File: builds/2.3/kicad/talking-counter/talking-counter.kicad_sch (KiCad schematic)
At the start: 16 parts, among them IC1 TLV3501AIDR, J1 Conn_Coaxial

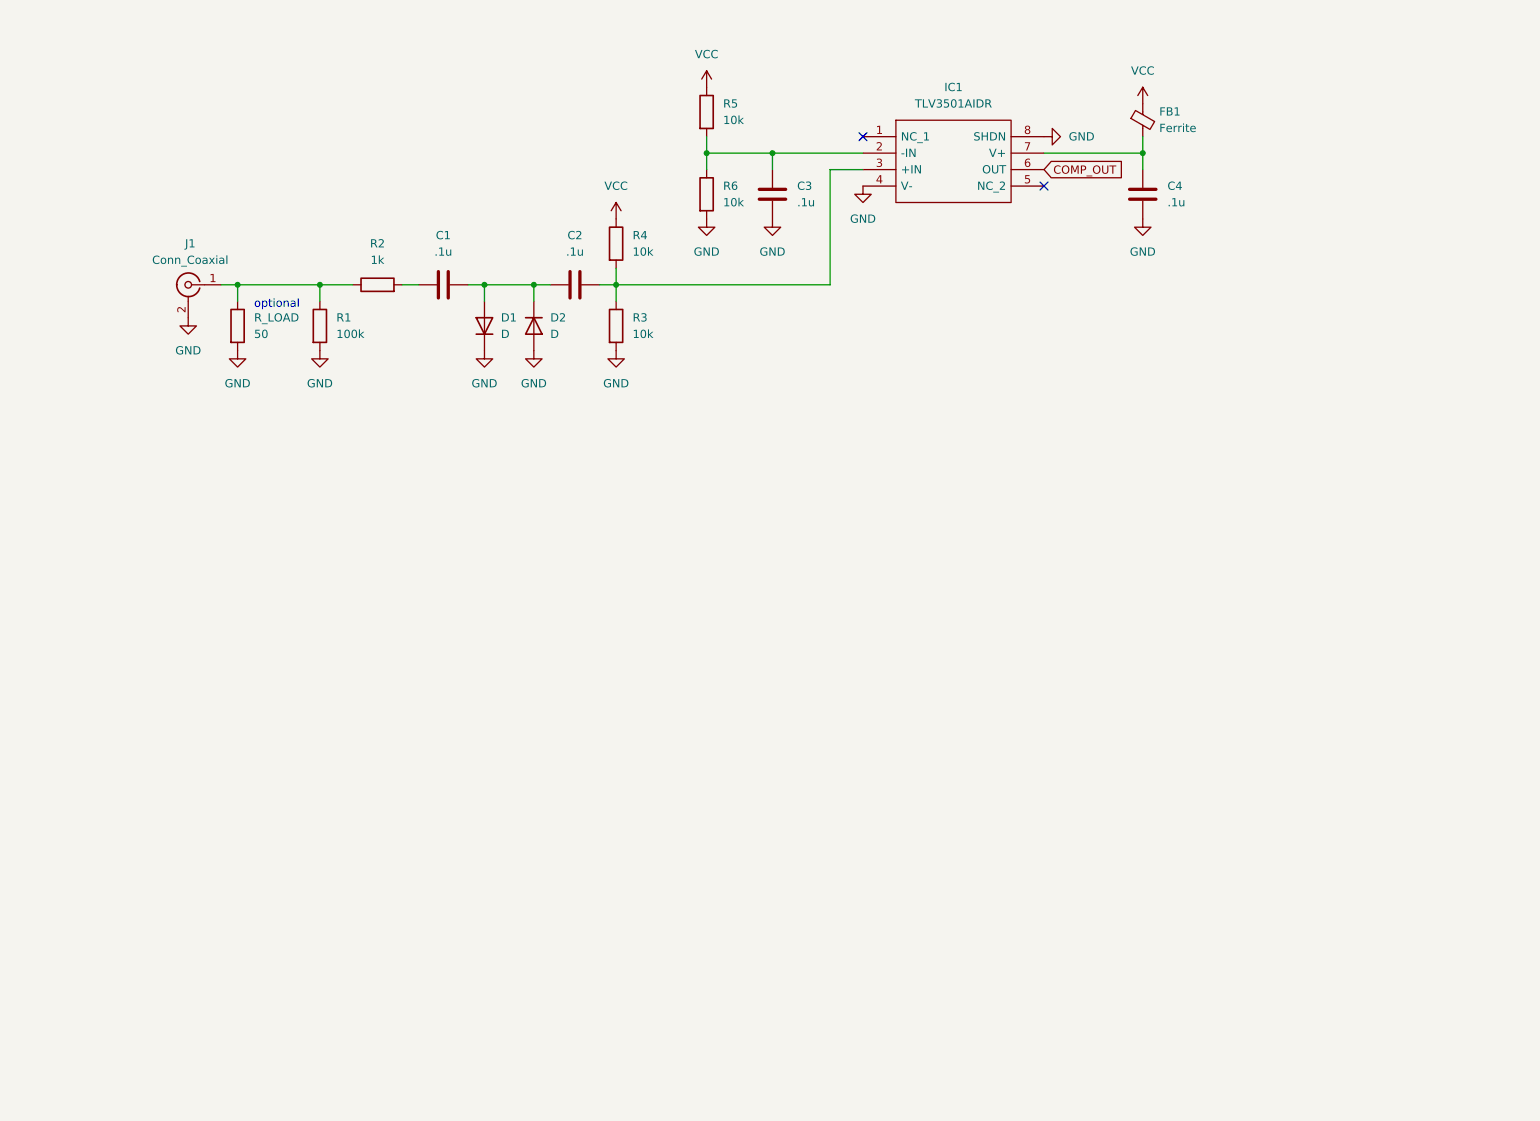
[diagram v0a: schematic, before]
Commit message: update schematic
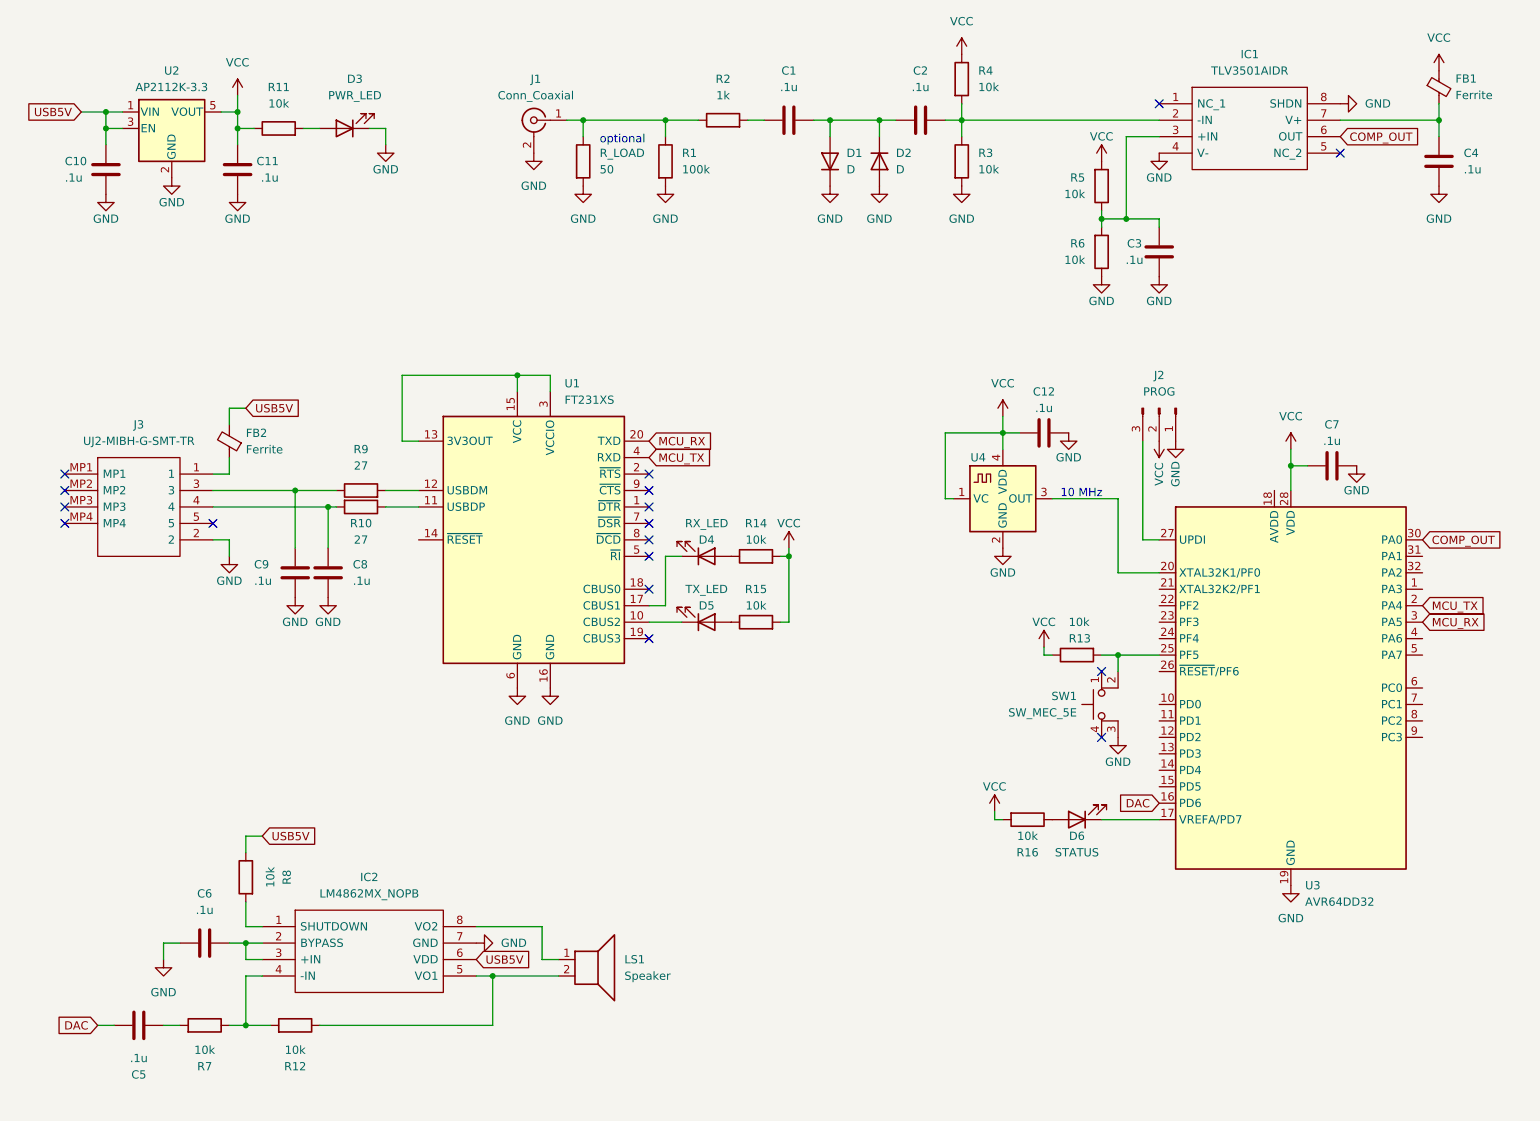
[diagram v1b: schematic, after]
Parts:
- added C10, C11, C12, C5, C6, C7, C8, C9: .1u, symbol Device:C
- added D3: PWR_LED, symbol Device:LED
- added D4: RX_LED, symbol Device:LED
- added D5: TX_LED, symbol Device:LED
- added D6: STATUS, symbol Device:LED
- added FB2: Ferrite, symbol Device:FerriteBead_Small
- added IC2: LM4862MX_NOPB, SOIC127P600X175-8N, symbol library loader:LM4862MX_NOPB
- added J2: PROG, symbol Connector:Conn_01x03_Pin
- added J3: UJ2-MIBH-G-SMT-TR, UJ2MIBHGSMTTR, symbol library loader:UJ2-MIBH-G-SMT-TR
- added LS1: Speaker, symbol Device:Speaker
- added R10, R9: 27, symbol Device:R
- added R11, R12, R13, R14, R15, R16, R7, R8: 10k, symbol Device:R
- added SW1: SW_MEC_5E, symbol Switch:SW_MEC_5E
- added U1: FT231XS, Package_SO:SSOP-20_3.9x8.7mm_P0.635mm, symbol Interface_USB:FT231XS
- added U2: AP2112K-3.3, Package_TO_SOT_SMD:SOT-23-5, symbol Regulator_Linear:AP2112K-3.3
- added U3: AVR64DD32, Package_QFP:TQFP-32_7x7mm_P0.8mm, symbol MCU_Microchip_AVR_Dx:AVR64DA32x-xPT
- added U4: FT5HV, Oscillator:Oscillator_SMD_Fox_FT5H_5.0x3.2mm, symbol Oscillator:FT5HV
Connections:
- net COMP_OUT: now also U3.30 (PA0)
- net GND: now also C3.2, R6.1, C10.1, C11.1, C12.1, C6.2, C7.1, C8.2, C9.1, D3.1 (K), IC2.7 (GND), J2.1 (Pin_1), J3.2, SW1.3 (K), U1.16 (GND), U1.6 (GND), U2.2 (GND), U3.19 (GND), U3.29 (GND), U4.2 (GND); no longer C3.1, R6.2
- net VCC: now also R5.2, C11.2, C12.2, C7.2, J2.2 (Pin_2), R11.1, R13.1, R14.2, R15.2, R16.2, U2.5 (VOUT), U3.28 (VDD), U4.1 (VC), U4.4 (VDD); no longer R5.1
- net at C2.1, R3.1, R4.2: now also IC1.2 (-IN); no longer IC1.3 (+IN)
- new net: D3.2 (A), R11.2
- new net: D4.2 (A), R14.1
- new net: C3.1, IC1.3 (+IN), R5.1, R6.2
- new net: D6.1 (K), U3.17 (VREFA/PD7)
- new net: D6.2 (A), R16.1
- new net: R10.1, U1.11 (USBDP)
- new net: C8.1, J3.4, R10.2
- new net: U3.20 (XTAL32K1/PF0), U4.3 (OUT)
- new net: R13.2, SW1.2, U3.25 (PF5)
- new net: J2.3 (Pin_3), U3.27 (UPDI)
- new net: IC2.5 (VO1), LS1.2, R12.1
- new net: IC2.4 (-IN), R12.2, R7.1
- new net: D5.1 (K), U1.10 (CBUS2)
- new net: R9.2, U1.12 (USBDM)
- new net: U1.13 (3V3OUT), U1.15 (VCC), U1.3 (VCCIO)
- new net: D4.1 (K), U1.17 (CBUS1)
- new net: FB2.1, J3.1
- new net: D5.2 (A), R15.1
- new net: C6.1, IC2.2 (BYPASS), IC2.3 (+IN)
- new net: IC2.1 (SHUTDOWN), R8.2
- new net: C9.2, J3.3, R9.1
- new net: IC2.8 (VO2), LS1.1
- new net: C5.1, R7.2
- new net DAC: C5.2, U3.16 (PD6)
- new net MCU_RX: U1.20 (TXD), U3.3 (PA5)
- new net MCU_TX: U1.4 (RXD), U3.2 (PA4)
- new net USB5V: C10.2, FB2.2, IC2.6 (VDD), R8.1, U2.1 (VIN), U2.3 (EN)
- no-connect marks 2 -> 17
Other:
- note added: "10 MHz"
- moved on the sheet: C1, C2, C3, C4, D1, D2, FB1, IC1, J1, R1, R2, R3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

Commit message: update schematic
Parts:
- added C13, C14, C16: .1u, symbol Device:C
- added D7: LED_SIG, symbol Device:LED
- added R17: 10k, symbol Device:R
- added RV1: R_VOL, symbol Device:R_Potentiometer
- added TP1: CKOUT, symbol Connector:TestPoint
- added TP2: 10MHz, symbol Connector:TestPoint
- C8, C9: value .1u -> 47p
- D3: value PWR_LED -> LED_PWR
- J3: value UJ2-MIBH-G-SMT-TR -> USBC
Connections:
- net COMP_OUT: now also C14.2
- net DAC: now also RV1.1; no longer C5.2
- net GND: now also C13.1, C16.1, D7.1 (K), RV1.3
- net USB5V: now also FB2.1, U1.15 (VCC), C13.2; no longer FB2.2
- net VCC: now also U1.14 (~{RESET}), U1.3 (VCCIO)
- net at U3.20 (XTAL32K1/PF0), U4.3 (OUT): now also TP2.1
- net at U3.5 (PA7): now also TP1.1
- net at J3.1: now also FB2.2, C16.2; no longer FB2.1
- new net: C14.1, R17.1
- new net: C5.2, RV1.2
- new net: D7.2 (A), R17.2
- now unconnected: U1.13 (3V3OUT)
- no-connect marks 17 -> 18
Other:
- note removed: "10 MHz"
- moved on the sheet: C4, FB1, FB2

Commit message: fix erc issues
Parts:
- J3: value USBC -> micro usb
- renumbered R_LOAD to R_LOAD1
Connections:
- net USB5V renamed +5V
- no-connect marks 18 -> 38

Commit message: update footprints
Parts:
- C1, C10, C11, C12, C13, C14, C16, C2, C3, C4, C5, C6, C7, C8, C9: footprint (none) -> Capacitor_SMD:C_0805_2012Metric_Pad1.18x1.45mm_HandSolder
- D1, D2: footprint (none) -> Diode_SMD:D_SOD-123
- D3, D4, D5, D7: footprint (none) -> LED_SMD:LED_0805_2012Metric_Pad1.15x1.40mm_HandSolder
- D6: value STATUS -> LED_STATUS; footprint (none) -> LED_SMD:LED_0805_2012Metric_Pad1.15x1.40mm_HandSolder
- FB1, FB2: footprint (none) -> Inductor_SMD:L_0805_2012Metric_Pad1.15x1.40mm_HandSolder
- IC1, IC2: footprint SOIC127P600X175-8N -> Package_SO:SOIC-8-1EP_3.9x4.9mm_P1.27mm_EP2.29x3mm
- J1: footprint (none) -> Connector_Coaxial:SMA_Amphenol_132134_Vertical
- J2: footprint (none) -> Connector_PinHeader_2.54mm:PinHeader_1x03_P2.54mm_Vertical
- J3: value micro usb -> UJ2-MIBH-G-SMT-TR; footprint UJ2MIBHGSMTTR -> Connector_USB:USB_Micro-B_Amphenol_10118193-0001LF_Horizontal

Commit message: custom speaker symbol
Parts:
- LS1: footprint (none) -> Library:speaker SM231508
- R1, R10, R11, R12, R13, R14, R15, R16, R17, R2, R3, R4, R5, R6, R7, R8, R9: footprint (none) -> Resistor_SMD:R_0805_2012Metric_Pad1.20x1.40mm_HandSolder
- RV1: footprint (none) -> Potentiometer_THT:Potentiometer_Alpha_RD901F-40-00D_Single_Vertical
- R_LOAD1: footprint (none) -> Resistor_THT:R_Axial_DIN0411_L9.9mm_D3.6mm_P20.32mm_Horizontal
- SW1: footprint (none) -> Button_Switch_THT:SW_PUSH_6mm_H5mm
- TP1, TP2: footprint (none) -> TestPoint:TestPoint_Pad_D1.0mm
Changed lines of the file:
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@@
       (effects (font (size 1.27 1.27)))
     )
-    (property "Footprint" "" (at 133.35 102.108 90)
+    (property "Footprint" "Resistor_SMD:R_0805_2012Metric_Pad1.20x1.40mm_HandSolder" (at 133.35 102.108 90)
       (effects (font (size 1.27 1.27)) hide)
     )
@@
       (effects (font (size 1.27 1.27)) (justify left))
     )
-    (property "Footprint" "" (at 104.902 39.37 90)
+    (property "Footprint" "Resistor_THT:R_Axial_DIN0411_L9.9mm_D3.6mm_P20.32mm_Horizontal" (at 104.902 39.37 90)
       (effects (font (size 1.27 1.27)) hide)
     )
@@
       (effects (font (size 1.27 1.27)) (justify right))
     )
-    (property "Footprint" "" (at 184.912 53.34 90)
+    (property "Footprint" "Resistor_SMD:R_0805_2012Metric_Pad1.20x1.40mm_HandSolder" (at 184.912 53.34 90)
       (effects (font (size 1.27 1.27)) hide)
     )
@@
       (effects (font (size 1.27 1.27)))
     )
-    (property "Footprint" "" (at 72.39 90.932 90)
+    (property "Footprint" "Resistor_SMD:R_0805_2012Metric_Pad1.20x1.40mm_HandSolder" (at 72.39 90.932 90)
       (effects (font (size 1.27 1.27)) hide)
     )
@@
       (effects (font (size 1.27 1.27)))
     )
-    (property "Footprint" "" (at 175.26 139.192 90)
+    (property "Footprint" "Resistor_SMD:R_0805_2012Metric_Pad1.20x1.40mm_HandSolder" (at 175.26 139.192 90)
       (effects (font (size 1.27 1.27)) hide)
     )
@@
       (effects (font (size 1.27 1.27)))
     )
-    (property "Footprint" "" (at 62.23 174.498 90)
+    (property "Footprint" "Resistor_SMD:R_0805_2012Metric_Pad1.20x1.40mm_HandSolder" (at 62.23 174.498 90)
       (effects (font (size 1.27 1.27)) hide)
     )
@@
       (effects (font (size 1.27 1.27)))
     )
-    (property "Footprint" "" (at 128.27 34.798 90)
+    (property "Footprint" "Resistor_SMD:R_0805_2012Metric_Pad1.20x1.40mm_HandSolder" (at 128.27 34.798 90)
       (effects (font (size 1.27 1.27)) hide)
     )
@@
       (effects (font (size 1.27 1.27)))
     )
-    (property "Footprint" "" (at 133.35 112.268 90)
+    (property "Footprint" "Resistor_SMD:R_0805_2012Metric_Pad1.20x1.40mm_HandSolder" (at 133.35 112.268 90)
       (effects (font (size 1.27 1.27)) hide)
     )
@@
       (effects (font (size 1.27 1.27)))
     )
-    (property "Footprint" "" (at 56.388 149.86 90)
+    (property "Footprint" "Resistor_SMD:R_0805_2012Metric_Pad1.20x1.40mm_HandSolder" (at 56.388 149.86 90)
       (effects (font (size 1.27 1.27)) hide)
     )
@@
       (effects (font (size 1.27 1.27)) (justify left))
     )
-    (property "Footprint" "" (at 107.95 167.64 0)
+    (property "Footprint" "Library:speaker SM231508" (at 107.95 167.64 0)
       (effects (font (size 1.27 1.27)) hide)
     )
@@
       (effects (font (size 1.27 1.27)) (justify right))
     )
-    (property "Footprint" "" (at 27.94 172.72 0)
+    (property "Footprint" "Potentiometer_THT:Potentiometer_Alpha_RD901F-40-00D_Single_Vertical" (at 27.94 172.72 0)
       (effects (font (size 1.27 1.27)) hide)
     )
@@
       (effects (font (size 1.27 1.27)) (justify left))
     )
-    (property "Footprint" "" (at 181.61 123.19 0)
+    (property "Footprint" "Button_Switch_THT:SW_PUSH_6mm_H5mm" (at 181.61 123.19 0)
       (effects (font (size 1.27 1.27)) hide)
     )
@@
       (effects (font (size 1.27 1.27)) (justify right))
     )
-    (property "Footprint" "" (at 237.49 118.11 0)
+    (property "Footprint" "TestPoint:TestPoint_Pad_D1.0mm" (at 237.49 118.11 0)
       (effects (font (size 1.27 1.27)) hide)
     )
@@
       (effects (font (size 1.27 1.27)))
     )
-    (property "Footprint" "" (at 185.42 97.79 0)
+    (property "Footprint" "TestPoint:TestPoint_Pad_D1.0mm" (at 185.42 97.79 0)
       (effects (font (size 1.27 1.27)) hide)
     )
@@
       (effects (font (size 1.27 1.27)) (justify right))
     )
-    (property "Footprint" "" (at 184.912 43.18 90)
+    (property "Footprint" "Resistor_SMD:R_0805_2012Metric_Pad1.20x1.40mm_HandSolder" (at 184.912 43.18 90)
       (effects (font (size 1.27 1.27)) hide)
     )
@@
       (effects (font (size 1.27 1.27)))
     )
-    (property "Footprint" "" (at 224.282 49.53 90)
+    (property "Footprint" "Resistor_SMD:R_0805_2012Metric_Pad1.20x1.40mm_HandSolder" (at 224.282 49.53 90)
       (effects (font (size 1.27 1.27)) hide)
     )
@@
       (effects (font (size 1.27 1.27)))
     )
-    (property "Footprint" "" (at 48.26 174.498 90)
+    (property "Footprint" "Resistor_SMD:R_0805_2012Metric_Pad1.20x1.40mm_HandSolder" (at 48.26 174.498 90)
       (effects (font (size 1.27 1.27)) hide)
     )
@@
       (effects (font (size 1.27 1.27)) (justify right))
     )
-    (property "Footprint" "" (at 182.88 113.792 90)
+    (property "Footprint" "Resistor_SMD:R_0805_2012Metric_Pad1.20x1.40mm_HandSolder" (at 182.88 113.792 90)
       (effects (font (size 1.27 1.27)) hide)
     )
@@
       (effects (font (size 1.27 1.27)))
     )
-    (property "Footprint" "" (at 59.69 36.068 90)
+    (property "Footprint" "Resistor_SMD:R_0805_2012Metric_Pad1.20x1.40mm_HandSolder" (at 59.69 36.068 90)
       (effects (font (size 1.27 1.27)) hide)
     )
@@
       (effects (font (size 1.27 1.27)) (justify left))
     )
-    (property "Footprint" "" (at 163.322 39.37 90)
+    (property "Footprint" "Resistor_SMD:R_0805_2012Metric_Pad1.20x1.40mm_HandSolder" (at 163.322 39.37 90)
       (effects (font (size 1.27 1.27)) hide)
     )
@@
       (effects (font (size 1.27 1.27)) (justify left))
     )
-    (property "Footprint" "" (at 163.322 26.67 90)
+    (property "Footprint" "Resistor_SMD:R_0805_2012Metric_Pad1.20x1.40mm_HandSolder" (at 163.322 26.67 90)
       (effects (font (size 1.27 1.27)) hide)
     )
@@
       (effects (font (size 1.27 1.27)))
     )
-    (property "Footprint" "" (at 72.39 91.948 90)
+    (property "Footprint" "Resistor_SMD:R_0805_2012Metric_Pad1.20x1.40mm_HandSolder" (at 72.39 91.948 90)
       (effects (font (size 1.27 1.27)) hide)
     )
@@
       (effects (font (size 1.27 1.27)) (justify left))
     )
-    (property "Footprint" "" (at 117.602 39.37 90)
-      (effects (font (size 1.27 1.27)) hide)
-    )
+    (property "Footprint" "Resistor_SMD:R_0805_2012Metric_Pad1.20x1.40mm_HandSolder" (at 117.602 39.37 90)
+      (effects (font (size 1.27 1.27)) hide)
+    )

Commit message: layout pcb
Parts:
- added H1, H2, H3, H4: MountingHole, MountingHole:MountingHole_4.3mm_M4_DIN965_Pad, symbol Mechanical:MountingHole
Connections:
- net GND: now also J2.3 (Pin_3); no longer J2.1 (Pin_1)
- net at U3.27 (UPDI): now also J2.1 (Pin_1); no longer J2.3 (Pin_3)
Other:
- moved on the sheet: J2
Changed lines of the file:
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@@
+    )
+  )
+  (symbol (lib_id "Mechanical:MountingHole") (at 155.575 167.64 0) (unit 1)
+    (in_bom yes) (on_board yes) (dnp no) (fields_autoplaced)
+    (property "Reference" "H1" (at 158.75 166.37 0)
+      (effects (font (size 1.27 1.27)) (justify left))
+    )
+    (property "Value" "MountingHole" (at 158.75 168.91 0)
+      (effects (font (size 1.27 1.27)) (justify left))
+    )
+    (property "Footprint" "MountingHole:MountingHole_4.3mm_M4_DIN965_Pad" (at 155.575 167.64 0)
+      (effects (font (size 1.27 1.27)) hide)
+    )
+    (property "Datasheet" "~" (at 155.575 167.64 0)
+      (effects (font (size 1.27 1.27)) hide)
+    )
+    (instances
+      (project "talking-counter"
+        (path "/bc948f24-ca1e-4e17-90c0-4fb791b09c5b"
+          (reference "H1") (unit 1)
+        )
+      )
     )
   )
@@
         (path "/bc948f24-ca1e-4e17-90c0-4fb791b09c5b"
           (reference "J1") (unit 1)
+        )
+      )
+    )
+  )
+  (symbol (lib_id "Mechanical:MountingHole") (at 155.575 172.72 0) (unit 1)
+    (in_bom yes) (on_board yes) (dnp no) (fields_autoplaced)
+    (property "Reference" "H2" (at 158.75 171.45 0)
+      (effects (font (size 1.27 1.27)) (justify left))
+    )
+    (property "Value" "MountingHole" (at 158.75 173.99 0)
+      (effects (font (size 1.27 1.27)) (justify left))
+    )
+    (property "Footprint" "MountingHole:MountingHole_4.3mm_M4_DIN965_Pad" (at 155.575 172.72 0)
+      (effects (font (size 1.27 1.27)) hide)
+    )
+    (property "Datasheet" "~" (at 155.575 172.72 0)
+      (effects (font (size 1.27 1.27)) hide)
+    )
+    (instances
+      (project "talking-counter"
+        (path "/bc948f24-ca1e-4e17-90c0-4fb791b09c5b"
+          (reference "H2") (unit 1)
         )
       )
@@
     )
   )
+  (symbol (lib_id "Mechanical:MountingHole") (at 155.575 182.88 0) (unit 1)
+    (in_bom yes) (on_board yes) (dnp no) (fields_autoplaced)
+    (property "Reference" "H4" (at 158.75 181.61 0)
+      (effects (font (size 1.27 1.27)) (justify left))
+    )
+    (property "Value" "MountingHole" (at 158.75 184.15 0)
+      (effects (font (size 1.27 1.27)) (justify left))
+    )
+    (property "Footprint" "MountingHole:MountingHole_4.3mm_M4_DIN965_Pad" (at 155.575 182.88 0)
+      (effects (font (size 1.27 1.27)) hide)
+    )
+    (property "Datasheet" "~" (at 155.575 182.88 0)
+      (effects (font (size 1.27 1.27)) hide)
+    )
+    (instances
+      (project "talking-counter"
+        (path "/bc948f24-ca1e-4e17-90c0-4fb791b09c5b"
+          (reference "H4") (unit 1)
+        )
+      )
+    )
+  )
   (symbol (lib_id "Device:R_Potentiometer") (at 27.94 172.72 0) (unit 1)
     (in_bom yes) (on_board yes) (dnp no) (fields_autoplaced)
@@
     )
   )
-  (symbol (lib_id "Connector:Conn_01x03_Pin") (at 195.58 77.47 270) (unit 1)
-    (in_bom yes) (on_board yes) (dnp no) (fields_autoplaced)
+  (symbol (lib_id "Connector:Conn_01x03_Pin") (at 195.58 77.47 90) (mirror x) (unit 1)
+    (in_bom yes) (on_board yes) (dnp no)
     (property "Reference" "J2" (at 195.58 72.39 90)
       (effects (font (size 1.27 1.27)))
@@
         )
       )
+    )
+  )
+  (symbol (lib_id "Mechanical:MountingHole") (at 155.575 177.8 0) (unit 1)
+    (in_bom yes) (on_board yes) (dnp no) (fields_autoplaced)
+    (property "Reference" "H3" (at 158.75 176.53 0)
+      (effects (font (size 1.27 1.27)) (justify left))
+    )
+    (property "Value" "MountingHole" (at 158.75 179.07 0)
+      (effects (font (size 1.27 1.27)) (justify left))
+    )
+    (property "Footprint" "MountingHole:MountingHole_4.3mm_M4_DIN965_Pad" (at 155.575 177.8 0)
+      (effects (font (size 1.27 1.27)) hide)
+    )
+    (property "Datasheet" "~" (at 155.575 177.8 0)
+      (effects (font (size 1.27 1.27)) hide)
+    )
+    (instances
+      (project "talking-counter"
+        (path "/bc948f24-ca1e-4e17-90c0-4fb791b09c5b"
+          (reference "H3") (unit 1)
+        )
+      )
